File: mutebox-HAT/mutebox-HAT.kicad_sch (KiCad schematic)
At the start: 17 parts, among them IC1 WM8804GEDS_V, J1 GPIO, U1 CAT24C256, U2 PCM1808PWR, Y1 12.288MHz

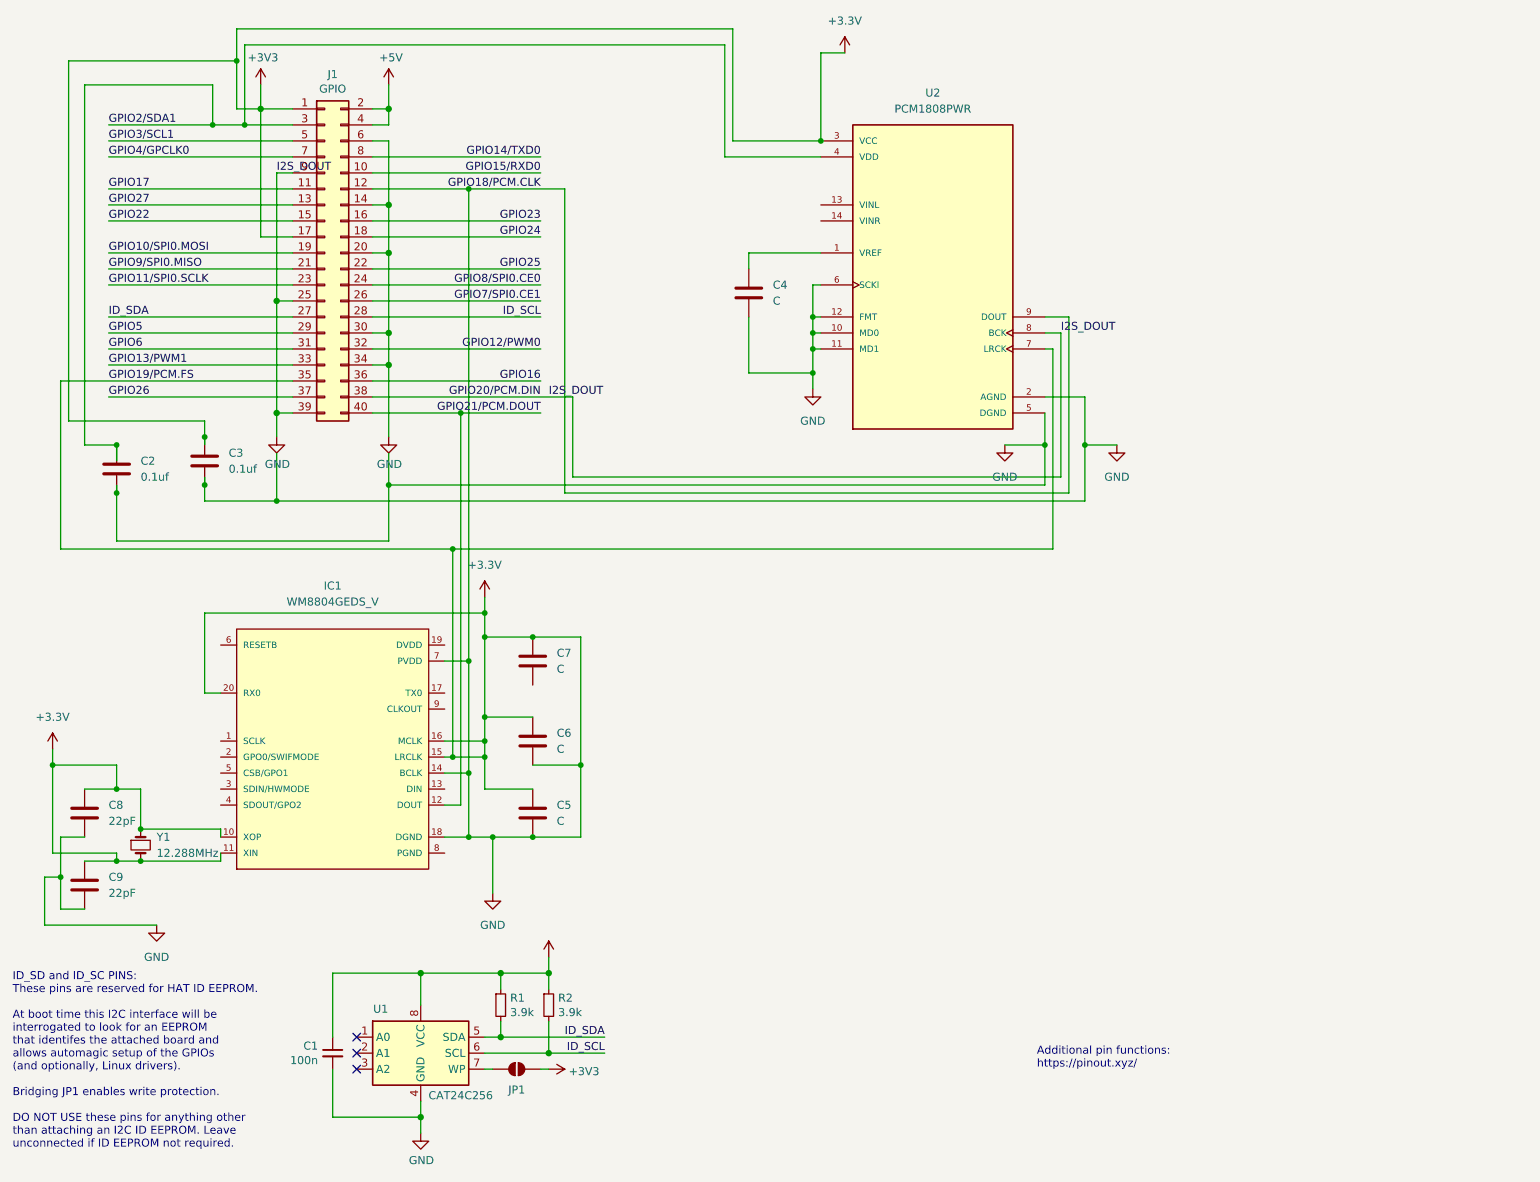
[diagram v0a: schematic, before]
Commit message: Finished connections between Pi and audio chips
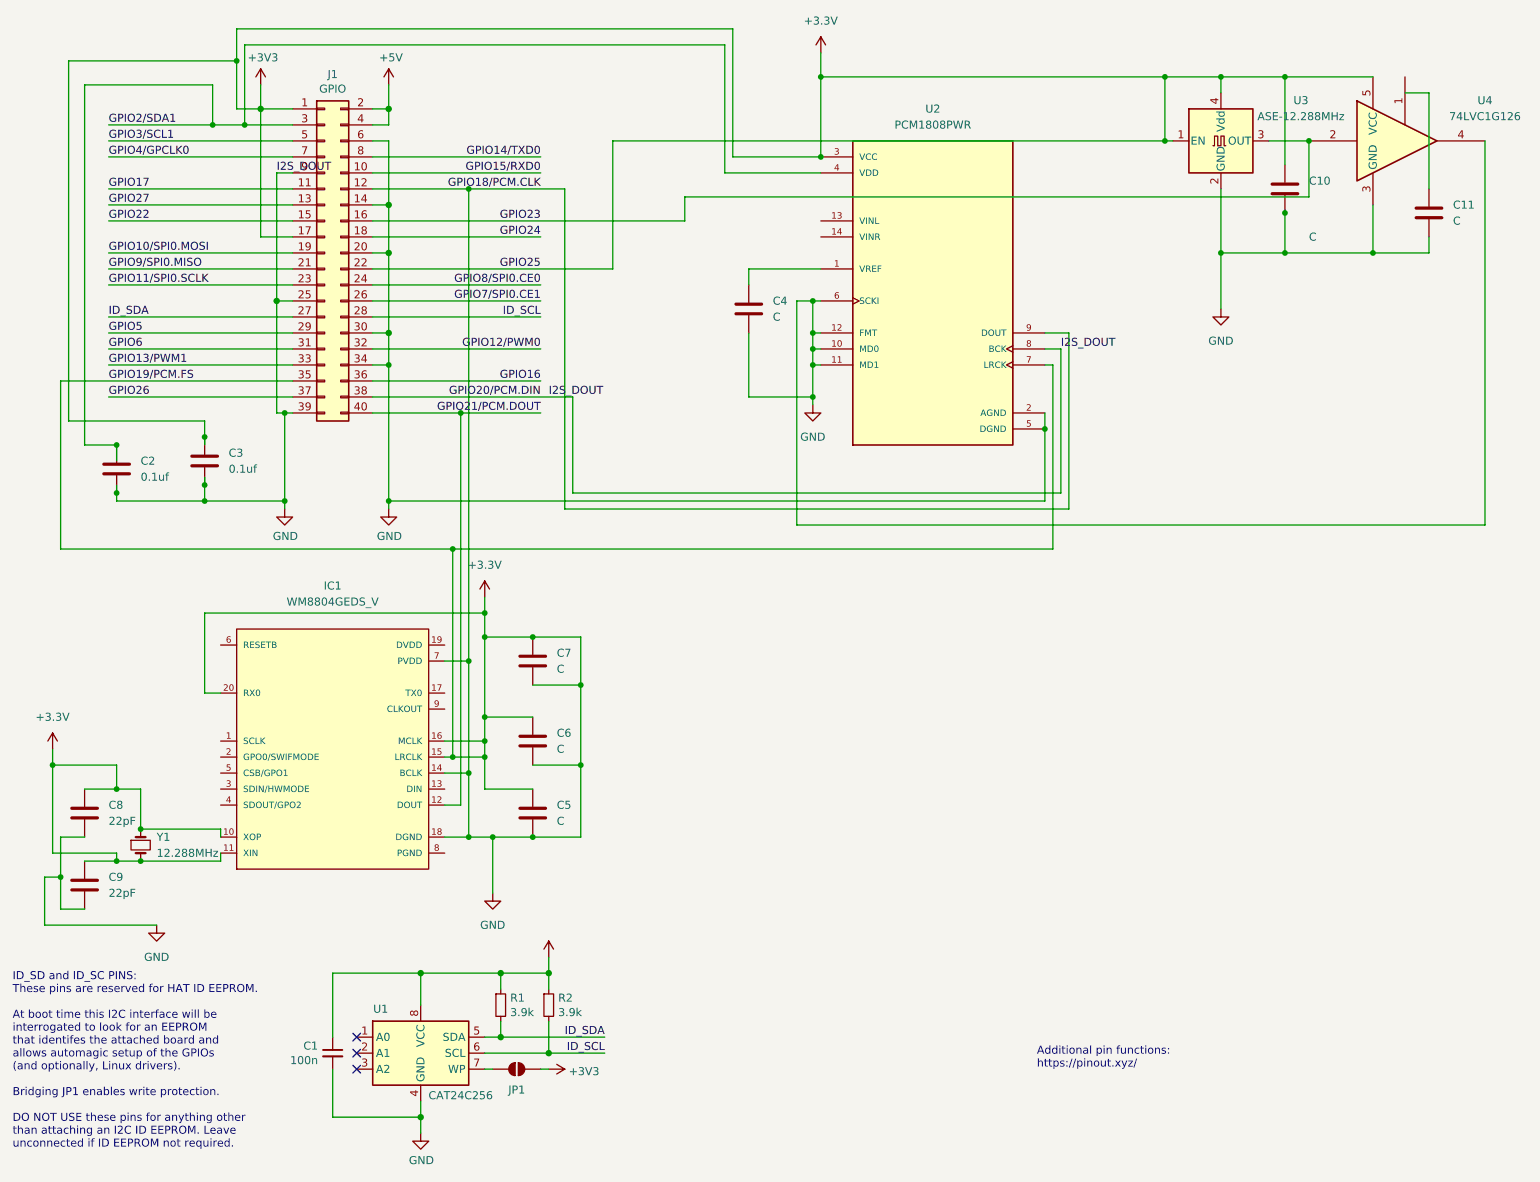
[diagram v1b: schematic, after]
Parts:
- added C10, C11: C, symbol Device:C
- added U3: ASE-12.288MHz, Oscillator:Oscillator_SMD_Abracon_ASE-4Pin_3.2x2.5mm, symbol Oscillator:ASE-xxxMHz
- added U4: 74LVC1G126, symbol 74xGxx:74LVC1G126
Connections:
- net GPIO25 is gone; now on net +3.3V: J1.22 (Pin_22)
- net +3.3V: now also C7.2, C10.1, C10.2, C11.2, U3.1 (EN), U3.2 (GND), U3.4 (Vdd), U4.3 (GND), U4.4, U4.5 (VCC)
- net GPIO23: now also U3.3 (OUT), U4.2
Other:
- moved on the sheet: C4, U2

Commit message: Complete schematic before complete rewrite
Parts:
- added C12: C, symbol Device:C
- added J2, J3: AudioJack2, symbol Connector_Audio:AudioJack2
- added J4: AFBR-2624Z, symbol Fiber_Optic:AFBR-2624Z
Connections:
- net +3.3V: now also C12.1, C12.2, J2.T, J3.T, J4.1 (Data_Out), J4.2 (VEER), J4.3 (VCCR), J4.5 (HP), J4.8 (HP)
- net at U2.13 (VINL): now also J2.S
- net at U2.14 (VINR): now also J3.S
